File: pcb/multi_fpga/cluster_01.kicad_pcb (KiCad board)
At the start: 2 copper layers, 161.3 x 208.8 mm, 52 parts, among them U25 Comment, U26 Comment, U27 Comment, U28 Comment, U29 Comment, U30 Comment, U31 Comment, U32 Comment, U33 Comment, U34 Comment, U35 Comment, U36 Comment, U37 Comment, U38 Comment, U39 Comment, U40 Comment, U41 Comment, U42 Comment, U43 Comment, U44 Comment, U45 Comment, U46 Comment, U47 Comment, U48 Comment

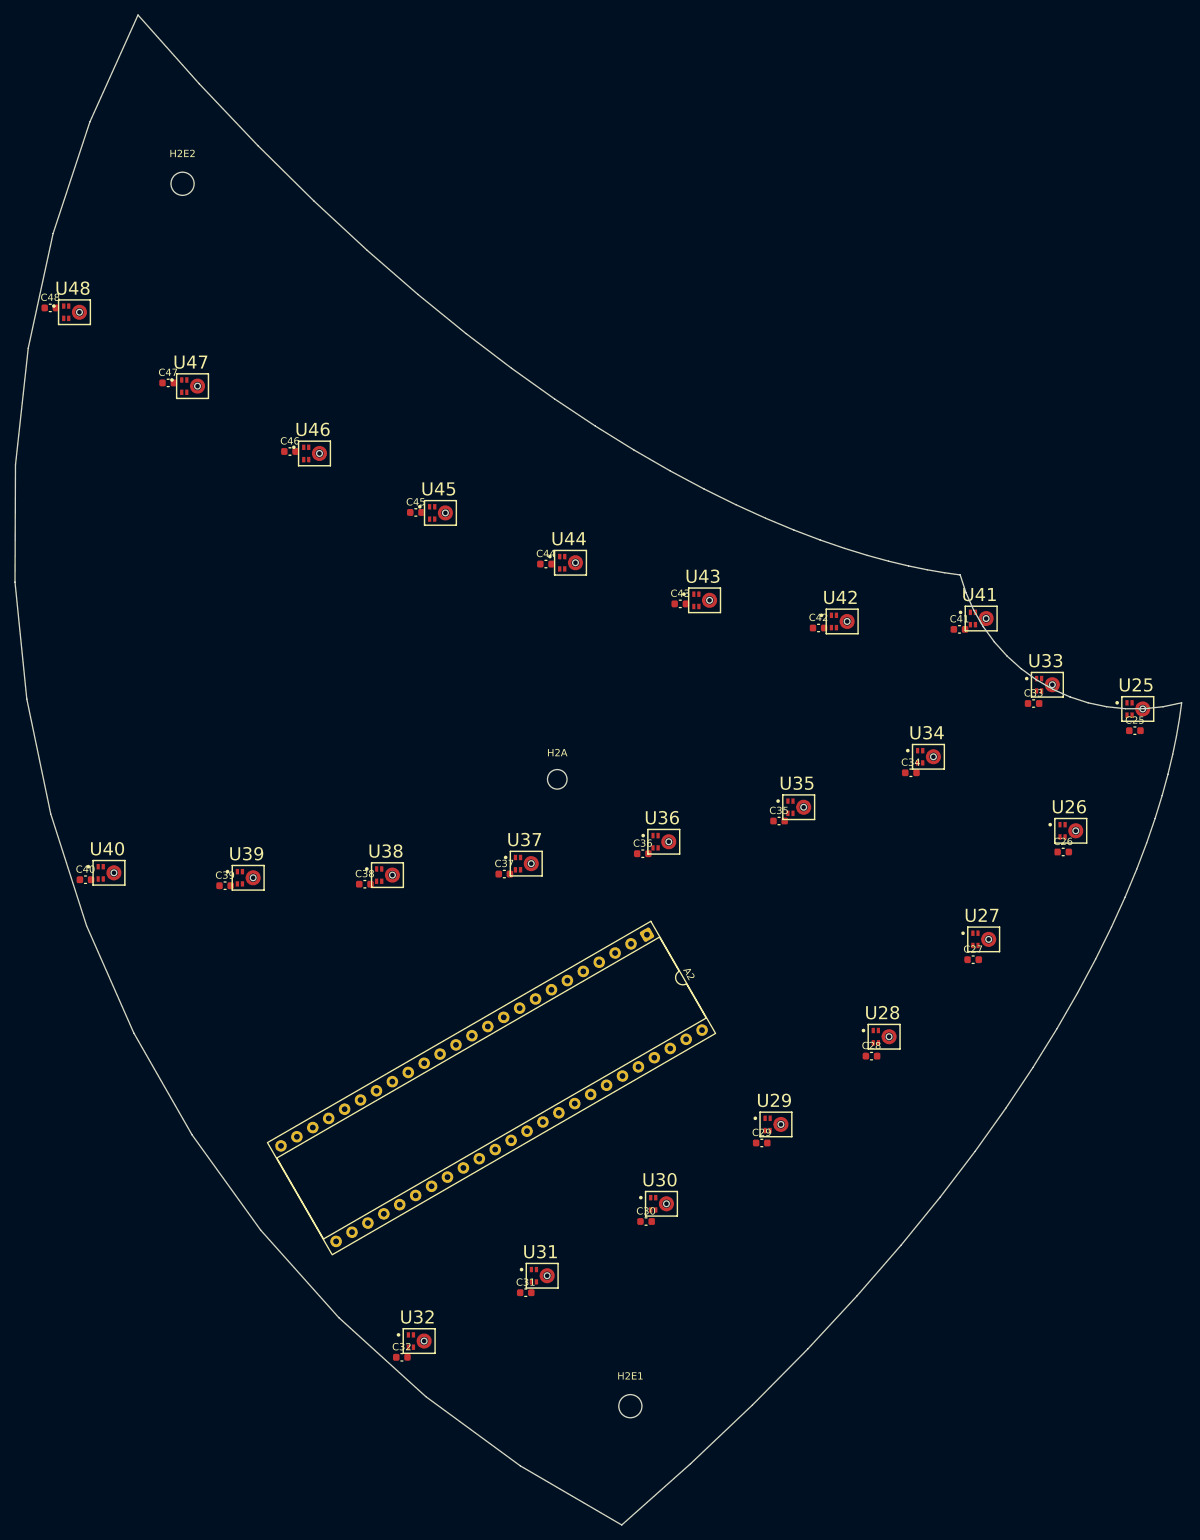
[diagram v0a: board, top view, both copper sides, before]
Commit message: Fixed inner circle of mics.
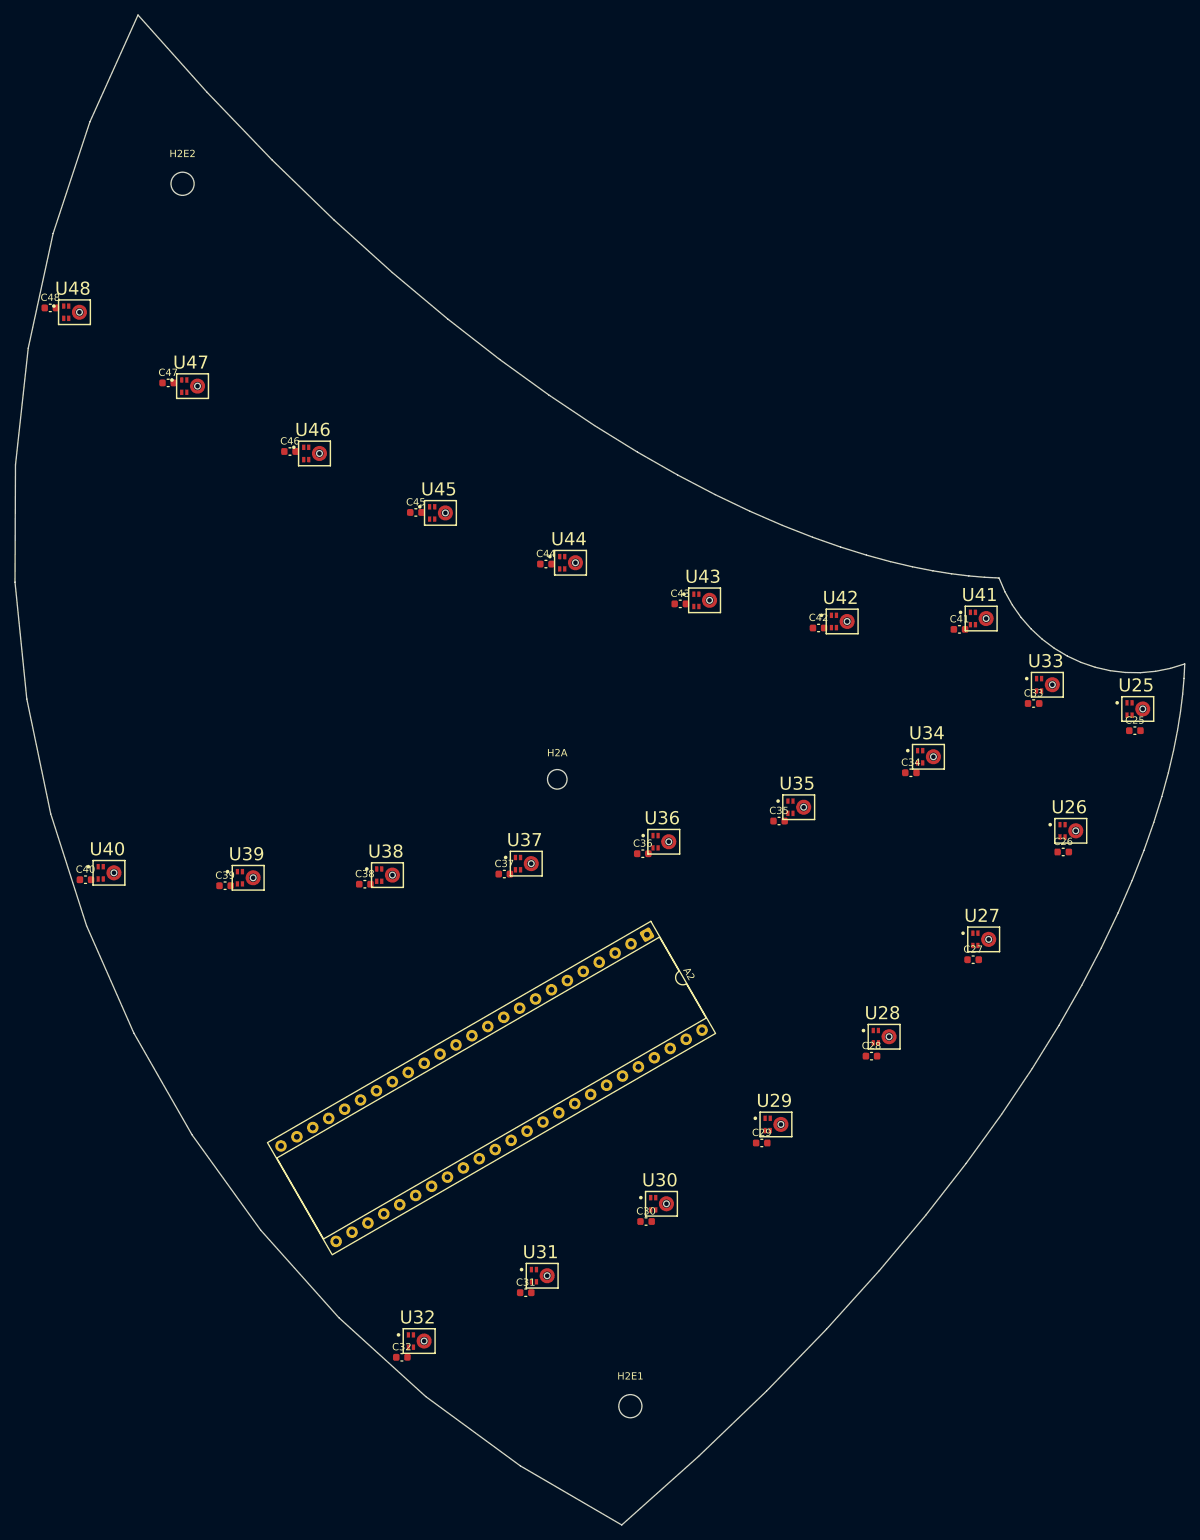
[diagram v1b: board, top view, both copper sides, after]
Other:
- board size 161.3 x 208.8 mm -> 161.7 x 208.8 mm
